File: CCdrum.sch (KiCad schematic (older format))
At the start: 28 parts, among them J1 USB_B_μ, J3 MIDI_out, J4 Program, U1 MSP430G2533, U2 AMS1117-3.3, U3 74AUP1G17

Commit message: Re-annotated components
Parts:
- R2: renamed from R7; value 1k -> RLED
- R3: renamed from R8; value 1k -> RLED
- R4: renamed from R11; value 1k -> RLED
- R5: renamed from R12; value 1k -> RLED
- R6: renamed from R13; value 1k -> RLED
- R7: renamed from R15; value 1k -> RLED
- renumbered D7 to D6, J4 to J2, R10 to R8
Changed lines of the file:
@@
 EESchema Schematic File Version 4
-LIBS:CCdrum-cache
 EELAYER 26 0
 EELAYER END
@@
 $EndComp
 $Comp
-L Device:R R7
+L Device:R R2
 U 1 1 5C783ECC
 P 6700 1950
-F 0 "R7" H 6770 1996 50  0000 L CNN
-F 1 "1k" H 6770 1905 50  0000 L CNN
+F 0 "R2" H 6770 1996 50  0000 L CNN
+F 1 "RLED" H 6770 1905 50  0000 L CNN
 F 2 "Resistor_THT:R_Axial_DIN0207_L6.3mm_D2.5mm_P7.62mm_Horizontal" V 6630 1950 50  0001 C CNN
 F 3 "~" H 6700 1950 50  0001 C CNN
@@
 $EndComp
 $Comp
-L Device:R R8
+L Device:R R3
 U 1 1 5C784A07
 P 7200 1950
-F 0 "R8" H 7270 1996 50  0000 L CNN
-F 1 "1k" H 7270 1905 50  0000 L CNN
+F 0 "R3" H 7270 1996 50  0000 L CNN
+F 1 "RLED" H 7270 1905 50  0000 L CNN
 F 2 "Resistor_THT:R_Axial_DIN0207_L6.3mm_D2.5mm_P7.62mm_Horizontal" V 7130 1950 50  0001 C CNN
 F 3 "~" H 7200 1950 50  0001 C CNN
@@
 $EndComp
 $Comp
-L Device:R R11
+L Device:R R4
 U 1 1 5C784C67
 P 7700 1950
-F 0 "R11" H 7770 1996 50  0000 L CNN
-F 1 "1k" H 7770 1905 50  0000 L CNN
+F 0 "R4" H 7770 1996 50  0000 L CNN
+F 1 "RLED" H 7770 1905 50  0000 L CNN
 F 2 "Resistor_THT:R_Axial_DIN0207_L6.3mm_D2.5mm_P7.62mm_Horizontal" V 7630 1950 50  0001 C CNN
 F 3 "~" H 7700 1950 50  0001 C CNN
@@
 $EndComp
 $Comp
-L Device:R R12
+L Device:R R5
 U 1 1 5C784E81
 P 8200 1950
-F 0 "R12" H 8270 1996 50  0000 L CNN
-F 1 "1k" H 8270 1905 50  0000 L CNN
+F 0 "R5" H 8270 1996 50  0000 L CNN
+F 1 "RLED" H 8270 1905 50  0000 L CNN
 F 2 "Resistor_THT:R_Axial_DIN0207_L6.3mm_D2.5mm_P7.62mm_Horizontal" V 8130 1950 50  0001 C CNN
 F 3 "~" H 8200 1950 50  0001 C CNN
@@
 $EndComp
 $Comp
-L Device:R R13
+L Device:R R6
 U 1 1 5C78509D
 P 8700 1950
-F 0 "R13" H 8770 1996 50  0000 L CNN
-F 1 "1k" H 8770 1905 50  0000 L CNN
+F 0 "R6" H 8770 1996 50  0000 L CNN
+F 1 "RLED" H 8770 1905 50  0000 L CNN
 F 2 "Resistor_THT:R_Axial_DIN0207_L6.3mm_D2.5mm_P7.62mm_Horizontal" V 8630 1950 50  0001 C CNN
 F 3 "~" H 8700 1950 50  0001 C CNN
@@
 LED_GAN
 $Comp
-L Device:LED D7
+L Device:LED D6
 U 1 1 5C786192
 P 9150 2250
-F 0 "D7" V 9188 2133 50  0000 R CNN
+F 0 "D6" V 9188 2133 50  0000 R CNN
 F 1 "ON" V 9097 2133 50  0000 R CNN
 F 2 "LED_SMD:LED_0805_2012Metric_Pad1.15x1.40mm_HandSolder" H 9150 2250 50  0001 C CNN
@@
 $EndComp
 $Comp
-L Device:R R15
+L Device:R R7
 U 1 1 5C786199
 P 9150 1950
-F 0 "R15" H 9220 1996 50  0000 L CNN
-F 1 "1k" H 9220 1905 50  0000 L CNN
+F 0 "R7" H 9220 1996 50  0000 L CNN
+F 1 "RLED" H 9220 1905 50  0000 L CNN
 F 2 "Resistor_THT:R_Axial_DIN0207_L6.3mm_D2.5mm_P7.62mm_Horizontal" V 9080 1950 50  0001 C CNN
 F 3 "~" H 9150 1950 50  0001 C CNN
@@
 $EndComp
 $Comp
-L Device:R R10
+L Device:R R8
 U 1 1 5C78C804
 P 7450 4150
-F 0 "R10" H 7520 4196 50  0000 L CNN
+F 0 "R8" H 7520 4196 50  0000 L CNN
 F 1 "68" H 7520 4105 50  0000 L CNN
 F 2 "Resistor_THT:R_Axial_DIN0207_L6.3mm_D2.5mm_P7.62mm_Horizontal" V 7380 4150 50  0001 C CNN
@@
 $EndComp
 $Comp
-L Connector_Generic:Conn_01x04 J4
+L Connector_Generic:Conn_01x04 J2
 U 1 1 5C7C23A3
 P 5950 3650
-F 0 "J4" H 6029 3642 50  0000 L CNN
+F 0 "J2" H 6029 3642 50  0000 L CNN
 F 1 "Program" H 6029 3551 50  0000 L CNN
 F 2 "Connector_PinHeader_2.54mm:PinHeader_1x04_P2.54mm_Vertical" H 5950 3650 50  0001 C CNN

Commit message: New Schematic
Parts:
- added RV6: 10k, w_pth_resistors:trimmer_alps-rk09k1130ah1, symbol Device:R_POT_US
- added SW1, SW2: SW_Push, Button_Switch_THT:SW_PUSH_6mm_H4.3mm, symbol Switch:SW_Push
- renumbered R9 to R8, R8 to R9
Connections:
- net labels added: LED_P1, LED_P2, LED_P3, LED_P4, LED_P5, LED_P6, PART, PUSH_L1, PUSH_L2
- net labels removed: LED_BIT, LED_DRV, LED_FLD, LED_GAN, LED_PAN, LED_STATUS
- wire segments 20 -> 22
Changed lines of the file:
@@
 EESchema Schematic File Version 4
+LIBS:CCdrum-cache
 EELAYER 26 0
 EELAYER END
@@
 Text GLabel 5050 2750 2    50   Input ~ 0
 PAN
-Text GLabel 5050 2550 2    50   Input ~ 0
+Text GLabel 5050 2650 2    50   Input ~ 0
 GAN
 $Comp
@@
 $EndComp
 Text GLabel 6700 1800 1    50   Input ~ 0
-LED_BIT
+LED_P1
 $Comp
 L Device:LED D2
@@
 $EndComp
 Text GLabel 7200 1800 1    50   Input ~ 0
-LED_FLD
+LED_P2
 $Comp
 L Device:LED D3
@@
 $EndComp
 Text GLabel 7700 1800 1    50   Input ~ 0
-LED_DRV
+LED_P3
 $Comp
 L Device:LED D4
@@
 $EndComp
 Text GLabel 8200 1800 1    50   Input ~ 0
-LED_PAN
+LED_P4
 $Comp
 L Device:LED D5
@@
 $EndComp
 Text GLabel 8700 1800 1    50   Input ~ 0
-LED_GAN
-Text GLabel 2050 3150 0    50   Input ~ 0
-LED_BIT
+LED_P5
+Text GLabel 2050 3050 0    50   Input ~ 0
+LED_P5
+Text GLabel 2050 2850 0    50   Input ~ 0
+LED_P3
+Text GLabel 2050 2750 0    50   Input ~ 0
+LED_P2
+Text GLabel 2050 2650 0    50   Input ~ 0
+LED_P1
 Text GLabel 2050 2950 0    50   Input ~ 0
-LED_FLD
-Text GLabel 2050 2850 0    50   Input ~ 0
-LED_DRV
-Text GLabel 2050 2750 0    50   Input ~ 0
-LED_PAN
-Text GLabel 2050 3050 0    50   Input ~ 0
-LED_GAN
+LED_P4
 $Comp
 L Device:LED D6
@@
 $EndComp
 Text GLabel 9150 1800 1    50   Input ~ 0
-LED_STATUS
-Text GLabel 2050 2650 0    50   Input ~ 0
-LED_STATUS
+LED_P6
+Text GLabel 2050 3150 0    50   Input ~ 0
+LED_P6
 Wire Wire Line
 	1300 3300 2050 3300
@@
 $EndComp
 $Comp
-L Device:R R8
+L Device:R R9
 U 1 1 5C78C804
 P 7450 4150
-F 0 "R8" H 7520 4196 50  0000 L CNN
+F 0 "R9" H 7520 4196 50  0000 L CNN
 F 1 "68" H 7520 4105 50  0000 L CNN
 F 2 "Resistor_THT:R_Axial_DIN0207_L6.3mm_D2.5mm_P7.62mm_Horizontal" V 7380 4150 50  0001 C CNN
@@
 	7450 4000 7450 3900
 $Comp
-L Device:R R9
+L Device:R R8
 U 1 1 5C78D68E
 P 8900 4300
-F 0 "R9" H 8970 4346 50  0000 L CNN
+F 0 "R8" H 8970 4346 50  0000 L CNN
 F 1 "68" H 8970 4255 50  0000 L CNN
 F 2 "Resistor_THT:R_Axial_DIN0207_L6.3mm_D2.5mm_P7.62mm_Horizontal" V 8830 4300 50  0001 C CNN
@@
 Text GLabel 5750 3750 0    50   Input ~ 0
 RST
+$Comp
+L Switch:SW_Push SW2
+U 1 1 5C9F877A
+P 2500 6050
+F 0 "SW2" V 2546 6002 50  0000 R CNN
+F 1 "SW_Push" V 2455 6002 50  0000 R CNN
+F 2 "Button_Switch_THT:SW_PUSH_6mm_H4.3mm" H 2500 6250 50  0001 C CNN
+F 3 "" H 2500 6250 50  0001 C CNN
+	1    2500 6050
+	0    -1   -1   0
+$EndComp
+$Comp
+L Switch:SW_Push SW1
+U 1 1 5C9F8BB9
+P 2500 5400
+F 0 "SW1" V 2546 5352 50  0000 R CNN
+F 1 "SW_Push" V 2455 5352 50  0000 R CNN
+F 2 "Button_Switch_THT:SW_PUSH_6mm_H4.3mm" H 2500 5600 50  0001 C CNN
+F 3 "" H 2500 5600 50  0001 C CNN
+	1    2500 5400
+	0    -1   -1   0
+$EndComp
+$Comp
+L power:GND #PWR0105
+U 1 1 5C9FA3CB
+P 2500 6250
+F 0 "#PWR0105" H 2500 6000 50  0001 C CNN
+F 1 "GND" H 2505 6077 50  0000 C CNN
+F 2 "" H 2500 6250 50  0001 C CNN
+F 3 "" H 2500 6250 50  0001 C CNN
+	1    2500 6250
+	1    0    0    -1
+$EndComp
+$Comp
+L power:GND #PWR0106
+U 1 1 5C9FA54A
+P 2500 5600
+F 0 "#PWR0106" H 2500 5350 50  0001 C CNN
+F 1 "GND" H 2505 5427 50  0000 C CNN
+F 2 "" H 2500 5600 50  0001 C CNN
+F 3 "" H 2500 5600 50  0001 C CNN
+	1    2500 5600
+	1    0    0    -1
+$EndComp
+$Comp
+L power:GND #PWR0107
+U 1 1 5C9FB89C
+P 3850 5850
+F 0 "#PWR0107" H 3850 5600 50  0001 C CNN
+F 1 "GND" H 3855 5677 50  0000 C CNN
+F 2 "" H 3850 5850 50  0001 C CNN
+F 3 "" H 3850 5850 50  0001 C CNN
+	1    3850 5850
+	1    0    0    -1
+$EndComp
+$Comp
+L power:+3.3V #PWR0108
+U 1 1 5C9FB8A2
+P 3850 5550
+F 0 "#PWR0108" H 3850 5400 50  0001 C CNN
+F 1 "+3.3V" H 3865 5723 50  0000 C CNN
+F 2 "" H 3850 5550 50  0001 C CNN
+F 3 "" H 3850 5550 50  0001 C CNN
+	1    3850 5550
+	1    0    0    -1
+$EndComp
+$Comp
+L Device:R_POT_US RV6
+U 1 1 5C9FB8A8
+P 3850 5700
+F 0 "RV6" H 3782 5746 50  0000 R CNN
+F 1 "10k" H 3782 5655 50  0000 R CNN
+F 2 "w_pth_resistors:trimmer_alps-rk09k1130ah1" H 3850 5700 50  0001 C CNN
+F 3 "~" H 3850 5700 50  0001 C CNN
+	1    3850 5700
+	1    0    0    -1
+$EndComp
+Text GLabel 4000 5700 2    50   Input ~ 0
+PART
+Text GLabel 5050 2550 2    50   Input ~ 0
+PART
+Text GLabel 2750 5200 2    50   Input ~ 0
+PUSH_L1
+Wire Wire Line
+	2750 5200 2500 5200
+Text GLabel 2700 5850 2    50   Input ~ 0
+PUSH_L2
+Wire Wire Line
+	2700 5850 2500 5850
 $EndSCHEMATC

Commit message: New PCB Arrangement
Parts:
- D1: value BIT -> 1
- D2: value FLD -> 2
- D3: value DRV -> 3
- D4: value PAN -> 4
- D5: value GAN -> 5
- D6: value ON -> 6
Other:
- note added: "To allow one-hand part modifications these should be single push and not hold to change layer mode 1/2/1+2"
- note added: "they need some sort of visual feedback on the leds"
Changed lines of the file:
@@
 L power:GND #PWR019
 U 1 1 5C781A9E
-P 3600 3900
-F 0 "#PWR019" H 3600 3650 50  0001 C CNN
-F 1 "GND" H 3605 3727 50  0000 C CNN
-F 2 "" H 3600 3900 50  0001 C CNN
-F 3 "" H 3600 3900 50  0001 C CNN
-	1    3600 3900
+P 3600 3750
+F 0 "#PWR019" H 3600 3500 50  0001 C CNN
+F 1 "GND" H 3605 3577 50  0000 C CNN
+F 2 "" H 3600 3750 50  0001 C CNN
+F 3 "" H 3600 3750 50  0001 C CNN
+	1    3600 3750
 	1    0    0    -1
 $EndComp
@@
 U 1 1 5C7800D8
 P 3550 2850
-F 0 "U1" H 3550 1922 50  0000 C CNN
-F 1 "MSP430G2533" H 3550 2013 50  0000 C CNN
+F 0 "U1" H 3700 2200 50  0000 C CNN
+F 1 "MSP430G2533" H 3200 2200 50  0000 C CNN
 F 2 "Package_DIP:DIP-20_W7.62mm" H 2350 2300 50  0001 C CIN
 F 3 "http://www.ti.com/lit/ds/symlink/msp430g2533.pdf" H 3600 2450 50  0001 C CNN
@@
 $EndComp
 Wire Wire Line
-	3600 3900 3600 3650
+	3600 3750 3600 3650
 $Comp
 L Device:LED D1
@@
 P 6700 2250
 F 0 "D1" V 6738 2133 50  0000 R CNN
-F 1 "BIT" V 6647 2133 50  0000 R CNN
+F 1 "1" V 6647 2133 50  0000 R CNN
 F 2 "LED_SMD:LED_0805_2012Metric_Pad1.15x1.40mm_HandSolder" H 6700 2250 50  0001 C CNN
 F 3 "~" H 6700 2250 50  0001 C CNN
@@
 P 7200 2250
 F 0 "D2" V 7238 2133 50  0000 R CNN
-F 1 "FLD" V 7147 2133 50  0000 R CNN
+F 1 "2" V 7147 2133 50  0000 R CNN
 F 2 "LED_SMD:LED_0805_2012Metric_Pad1.15x1.40mm_HandSolder" H 7200 2250 50  0001 C CNN
 F 3 "~" H 7200 2250 50  0001 C CNN
@@
 P 7700 2250
 F 0 "D3" V 7738 2133 50  0000 R CNN
-F 1 "DRV" V 7647 2133 50  0000 R CNN
+F 1 "3" V 7647 2133 50  0000 R CNN
 F 2 "LED_SMD:LED_0805_2012Metric_Pad1.15x1.40mm_HandSolder" H 7700 2250 50  0001 C CNN
 F 3 "~" H 7700 2250 50  0001 C CNN
@@
 P 8200 2250
 F 0 "D4" V 8238 2133 50  0000 R CNN
-F 1 "PAN" V 8147 2133 50  0000 R CNN
+F 1 "4" V 8147 2133 50  0000 R CNN
 F 2 "LED_SMD:LED_0805_2012Metric_Pad1.15x1.40mm_HandSolder" H 8200 2250 50  0001 C CNN
 F 3 "~" H 8200 2250 50  0001 C CNN
@@
 P 8700 2250
 F 0 "D5" V 8738 2133 50  0000 R CNN
-F 1 "GAN" V 8647 2133 50  0000 R CNN
+F 1 "5" V 8647 2133 50  0000 R CNN
 F 2 "LED_SMD:LED_0805_2012Metric_Pad1.15x1.40mm_HandSolder" H 8700 2250 50  0001 C CNN
 F 3 "~" H 8700 2250 50  0001 C CNN
@@
 P 9150 2250
 F 0 "D6" V 9188 2133 50  0000 R CNN
-F 1 "ON" V 9097 2133 50  0000 R CNN
+F 1 "6" V 9097 2133 50  0000 R CNN
 F 2 "LED_SMD:LED_0805_2012Metric_Pad1.15x1.40mm_HandSolder" H 9150 2250 50  0001 C CNN
 F 3 "~" H 9150 2250 50  0001 C CNN
@@
 Wire Wire Line
 	2700 5850 2500 5850
+Text Notes 1700 6700 0    50   ~ 0
+To allow one-hand part modifications these should be single push and not hold to change layer mode 1/2/1+2
+Text Notes 1500 6900 0    50   ~ 0
+they need some sort of visual feedback on the leds
 $EndSCHEMATC

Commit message: PCB Routed
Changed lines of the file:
@@
 Text Notes 1500 6900 0    50   ~ 0
 they need some sort of visual feedback on the leds
+Text GLabel 2050 2450 0    50   Input ~ 0
+PUSH_L1
+Text GLabel 2050 2550 0    50   Input ~ 0
+PUSH_L2
 $EndSCHEMATC

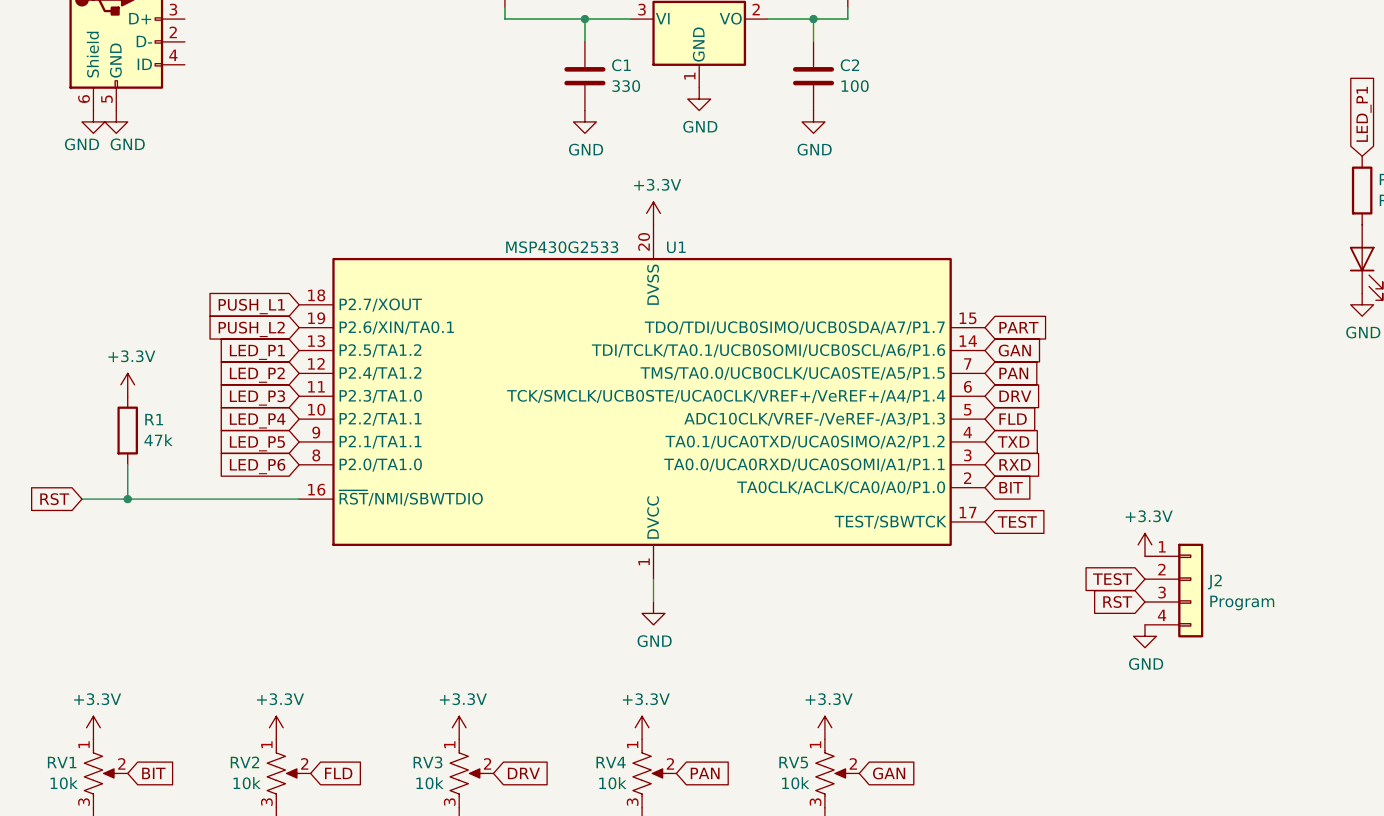
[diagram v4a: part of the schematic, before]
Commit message: Added Decoupling caps
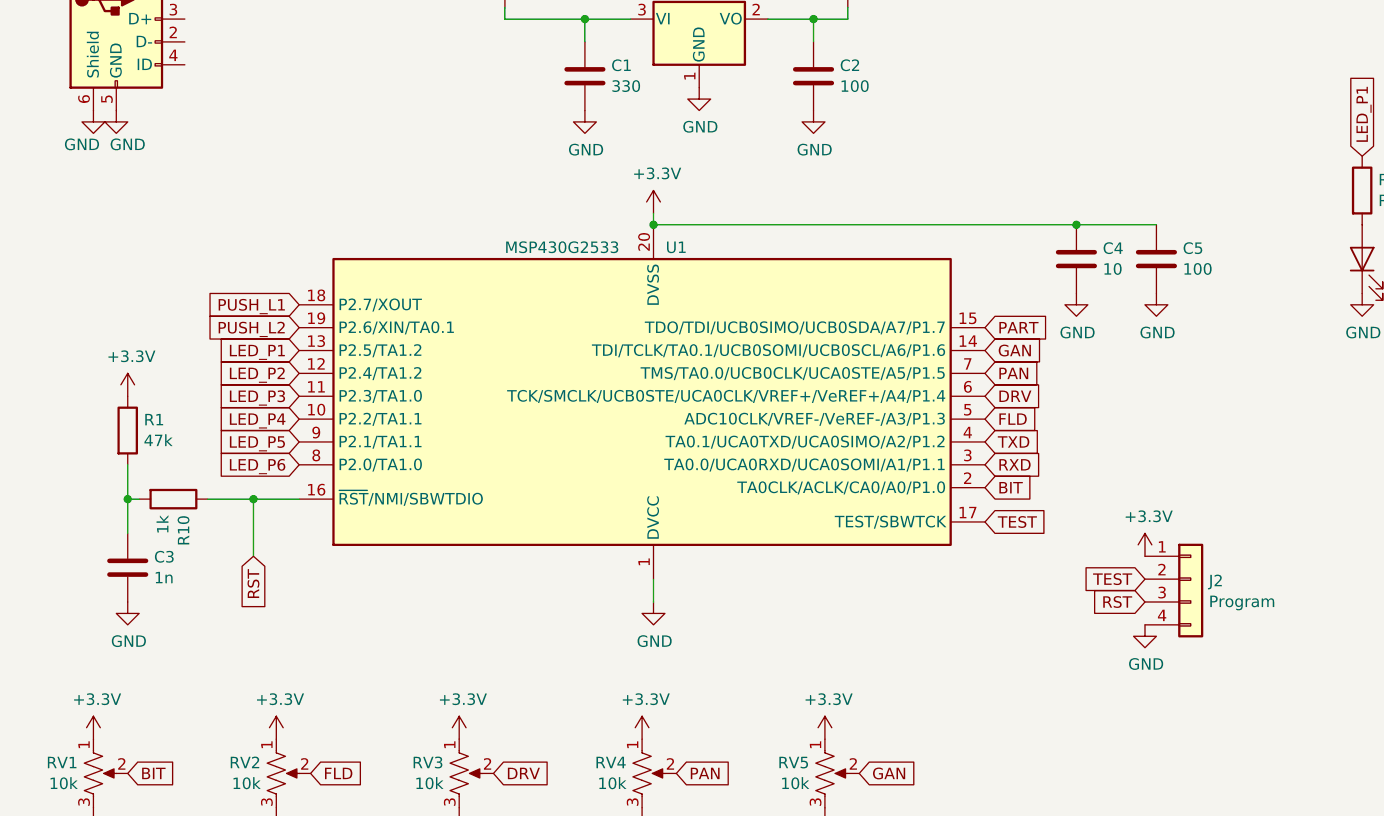
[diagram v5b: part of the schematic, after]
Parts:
- added C3: 1n, Capacitor_THT:C_Disc_D5.0mm_W2.5mm_P5.00mm, symbol Device:C
- added C4: 10, Capacitor_THT:C_Disc_D5.0mm_W2.5mm_P5.00mm, symbol Device:C
- added C5: 100, Capacitor_THT:C_Disc_D5.0mm_W2.5mm_P5.00mm, symbol Device:C
- added R10: 1k, Resistor_THT:R_Axial_DIN0207_L6.3mm_D2.5mm_P7.62mm_Horizontal, symbol Device:R
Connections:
- wire segments 22 -> 28
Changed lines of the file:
@@
 L power:+3.3V #PWR018
 U 1 1 5C781EB9
-P 3600 2100
-F 0 "#PWR018" H 3600 1950 50  0001 C CNN
-F 1 "+3.3V" H 3615 2273 50  0000 C CNN
-F 2 "" H 3600 2100 50  0001 C CNN
-F 3 "" H 3600 2100 50  0001 C CNN
-	1    3600 2100
+P 3600 2050
+F 0 "#PWR018" H 3600 1900 50  0001 C CNN
+F 1 "+3.3V" H 3615 2223 50  0000 C CNN
+F 2 "" H 3600 2050 50  0001 C CNN
+F 3 "" H 3600 2050 50  0001 C CNN
+	1    3600 2050
 	1    0    0    -1
 $EndComp
@@
 Text GLabel 2050 3150 0    50   Input ~ 0
 LED_P6
-Wire Wire Line
-	1300 3300 2050 3300
 $Comp
 L power:+5V #PWR013
@@
 Wire Wire Line
 	1300 3300 1300 3150
-Text GLabel 1100 3300 0    50   Input ~ 0
+Text GLabel 1850 3550 3    50   Input ~ 0
 RST
-Wire Wire Line
-	1100 3300 1300 3300
-Connection ~ 1300 3300
 Text GLabel 5750 3750 0    50   Input ~ 0
 RST
@@
 Text GLabel 2050 2550 0    50   Input ~ 0
 PUSH_L2
+$Comp
+L Device:R R10
+U 1 1 5CA092D9
+P 1500 3300
+F 0 "R10" H 1570 3346 50  0000 L CNN
+F 1 "1k" H 1570 3255 50  0000 L CNN
+F 2 "Resistor_THT:R_Axial_DIN0207_L6.3mm_D2.5mm_P7.62mm_Horizontal" V 1430 3300 50  0001 C CNN
+F 3 "~" H 1500 3300 50  0001 C CNN
+	1    1500 3300
+	0    1    1    0
+$EndComp
+Wire Wire Line
+	1350 3300 1300 3300
+Wire Wire Line
+	1650 3300 1850 3300
+Wire Wire Line
+	1850 3550 1850 3300
+Connection ~ 1850 3300
+Wire Wire Line
+	1850 3300 2050 3300
+$Comp
+L Device:C C3
+U 1 1 5CA0A90F
+P 1300 3600
+F 0 "C3" H 1415 3646 50  0000 L CNN
+F 1 "1n" H 1415 3555 50  0000 L CNN
+F 2 "Capacitor_THT:C_Disc_D5.0mm_W2.5mm_P5.00mm" H 1338 3450 50  0001 C CNN
+F 3 "~" H 1300 3600 50  0001 C CNN
+	1    1300 3600
+	1    0    0    -1
+$EndComp
+$Comp
+L power:GND #PWR?
+U 1 1 5CA0AC3E
+P 1300 3750
+F 0 "#PWR?" H 1300 3500 50  0001 C CNN
+F 1 "GND" H 1305 3577 50  0000 C CNN
+F 2 "" H 1300 3750 50  0001 C CNN
+F 3 "" H 1300 3750 50  0001 C CNN
+	1    1300 3750
+	1    0    0    -1
+$EndComp
+Wire Wire Line
+	1300 3450 1300 3300
+Connection ~ 1300 3300
+Wire Wire Line
+	3600 2050 3600 2100
+Wire Wire Line
+	3600 2100 5450 2100
+Connection ~ 3600 2100
+$Comp
+L Device:C C4
+U 1 1 5CA0BB5F
+P 5450 2250
+F 0 "C4" H 5565 2296 50  0000 L CNN
+F 1 "10" H 5565 2205 50  0000 L CNN
+F 2 "Capacitor_THT:C_Disc_D5.0mm_W2.5mm_P5.00mm" H 5488 2100 50  0001 C CNN
+F 3 "~" H 5450 2250 50  0001 C CNN
+	1    5450 2250
+	1    0    0    -1
+$EndComp
+Connection ~ 5450 2100
+Wire Wire Line
+	5450 2100 5800 2100
+$Comp
+L Device:C C5
+U 1 1 5CA0BBF9
+P 5800 2250
+F 0 "C5" H 5915 2296 50  0000 L CNN
+F 1 "100" H 5915 2205 50  0000 L CNN
+F 2 "Capacitor_THT:C_Disc_D5.0mm_W2.5mm_P5.00mm" H 5838 2100 50  0001 C CNN
+F 3 "~" H 5800 2250 50  0001 C CNN
+	1    5800 2250
+	1    0    0    -1
+$EndComp
+$Comp
+L power:GND #PWR?
+U 1 1 5CA0BC7E
+P 5450 2400
+F 0 "#PWR?" H 5450 2150 50  0001 C CNN
+F 1 "GND" H 5455 2227 50  0000 C CNN
+F 2 "" H 5450 2400 50  0001 C CNN
+F 3 "" H 5450 2400 50  0001 C CNN
+	1    5450 2400
+	1    0    0    -1
+$EndComp
+$Comp
+L power:GND #PWR?
+U 1 1 5CA0BCCF
+P 5800 2400
+F 0 "#PWR?" H 5800 2150 50  0001 C CNN
+F 1 "GND" H 5805 2227 50  0000 C CNN
+F 2 "" H 5800 2400 50  0001 C CNN
+F 3 "" H 5800 2400 50  0001 C CNN
+	1    5800 2400
+	1    0    0    -1
+$EndComp
 $EndSCHEMATC

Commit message: USB changed, small errors on board
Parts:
- J1: footprint Connector_USB:USB_Micro-B_GCT_USB3076-30-A -> w_conn_pc:conn_usb_B_micro_smd-2
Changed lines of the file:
@@
 F 0 "J1" H 1305 1667 50  0000 C CNN
 F 1 "USB_B_μ" H 1305 1576 50  0000 C CNN
-F 2 "Connector_USB:USB_Micro-B_GCT_USB3076-30-A" H 1400 1150 50  0001 C CNN
+F 2 "w_conn_pc:conn_usb_B_micro_smd-2" H 1400 1150 50  0001 C CNN
 F 3 "~" H 1400 1150 50  0001 C CNN
 	1    1250 1200
@@
 $EndComp
 $Comp
-L power:GND #PWR?
+L power:GND #PWR0109
 U 1 1 5CA0AC3E
 P 1300 3750
-F 0 "#PWR?" H 1300 3500 50  0001 C CNN
+F 0 "#PWR0109" H 1300 3500 50  0001 C CNN
 F 1 "GND" H 1305 3577 50  0000 C CNN
 F 2 "" H 1300 3750 50  0001 C CNN
@@
 $EndComp
 $Comp
-L power:GND #PWR?
+L power:GND #PWR0110
 U 1 1 5CA0BC7E
 P 5450 2400
-F 0 "#PWR?" H 5450 2150 50  0001 C CNN
+F 0 "#PWR0110" H 5450 2150 50  0001 C CNN
 F 1 "GND" H 5455 2227 50  0000 C CNN
 F 2 "" H 5450 2400 50  0001 C CNN
@@
 $EndComp
 $Comp
-L power:GND #PWR?
+L power:GND #PWR0111
 U 1 1 5CA0BCCF
 P 5800 2400
-F 0 "#PWR?" H 5800 2150 50  0001 C CNN
+F 0 "#PWR0111" H 5800 2150 50  0001 C CNN
 F 1 "GND" H 5805 2227 50  0000 C CNN
 F 2 "" H 5800 2400 50  0001 C CNN

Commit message: Removed comment text
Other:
- note removed: "To allow one-hand part modifications these should be single push and not hold to change layer mode 1/2/1+2"
- note removed: "they need some sort of visual feedback on the leds"
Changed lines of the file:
@@
 Wire Wire Line
 	2700 5850 2500 5850
-Text Notes 1700 6700 0    50   ~ 0
-To allow one-hand part modifications these should be single push and not hold to change layer mode 1/2/1+2
-Text Notes 1500 6900 0    50   ~ 0
-they need some sort of visual feedback on the leds
 Text GLabel 2050 2450 0    50   Input ~ 0
 PUSH_L1
